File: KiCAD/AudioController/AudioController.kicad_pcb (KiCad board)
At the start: 2 copper layers, 170 x 170 mm, 95 parts, among them J1 CS_1_H, J10 SD_3_CTRL, J11 8P8C, J12 CS_3_Measure, J13 CS_4_H, J14 SD_4_CTRL, J15 8P8C, J16 CS_4_Measure, J17 CS_5_H, J18 SD_5_CTRL, J19 8P8C, J2 SD_1_CTRL, J20 CS_5_Measure, J21 MOSI_H, J22 MOSI_Measure, J23 SCK_H, J24 SCK_Measure, J25 Power, J26 CS1_BR, J27 CS1_BR, J28 CS1_BR, J29 CS1_BR, J3 8P8C, J30 CS1_BR, J4 CS_1_Measure, J5 CS_2_H, J6 SD_2_CTRL, J7 8P8C, J8 CS_2_Measure, J9 CS_3_H, SW1 SW_Push, SW2 SW_Push, SW3 SW_Push, SW4 SW_Push, SW5 SW_Push, SW6 SW_Push, U1 ESP32-DevKitC, U2 ESP32-DevKitC

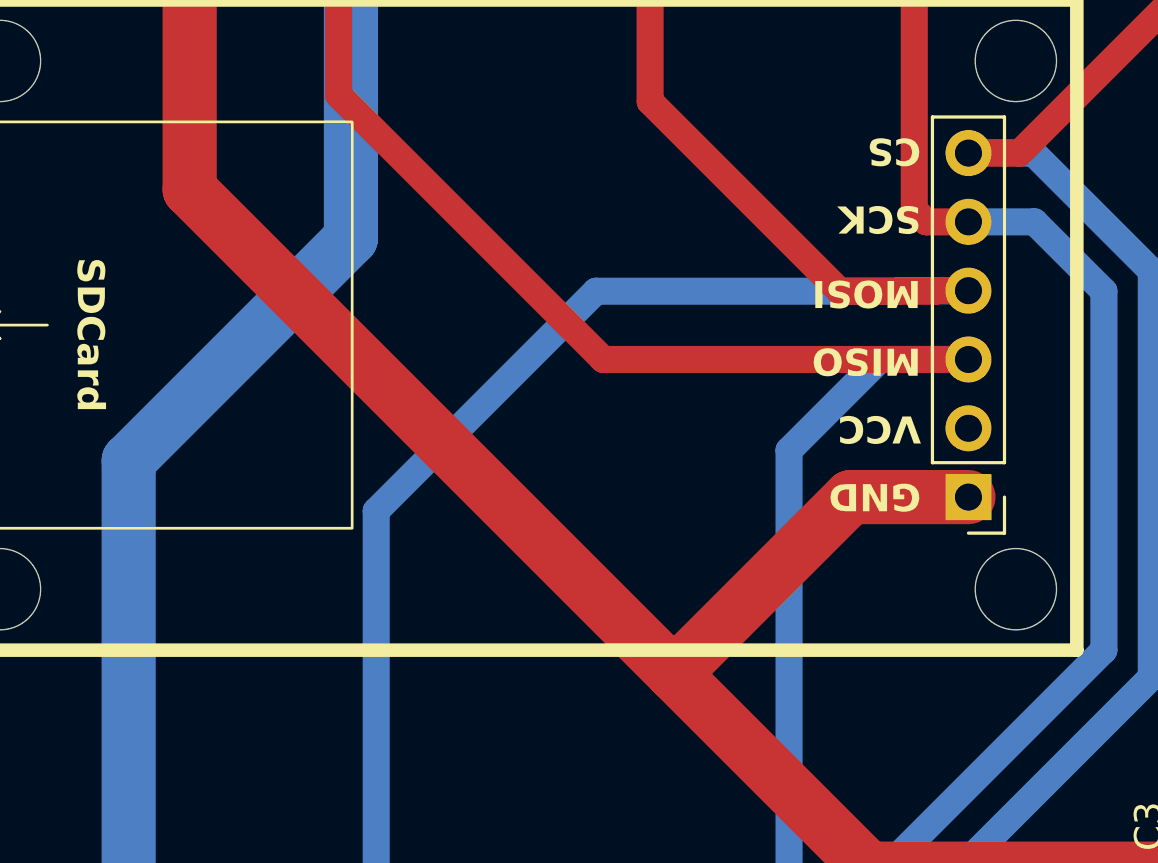
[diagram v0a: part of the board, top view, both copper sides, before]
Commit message: fixed pin assignment sd-card
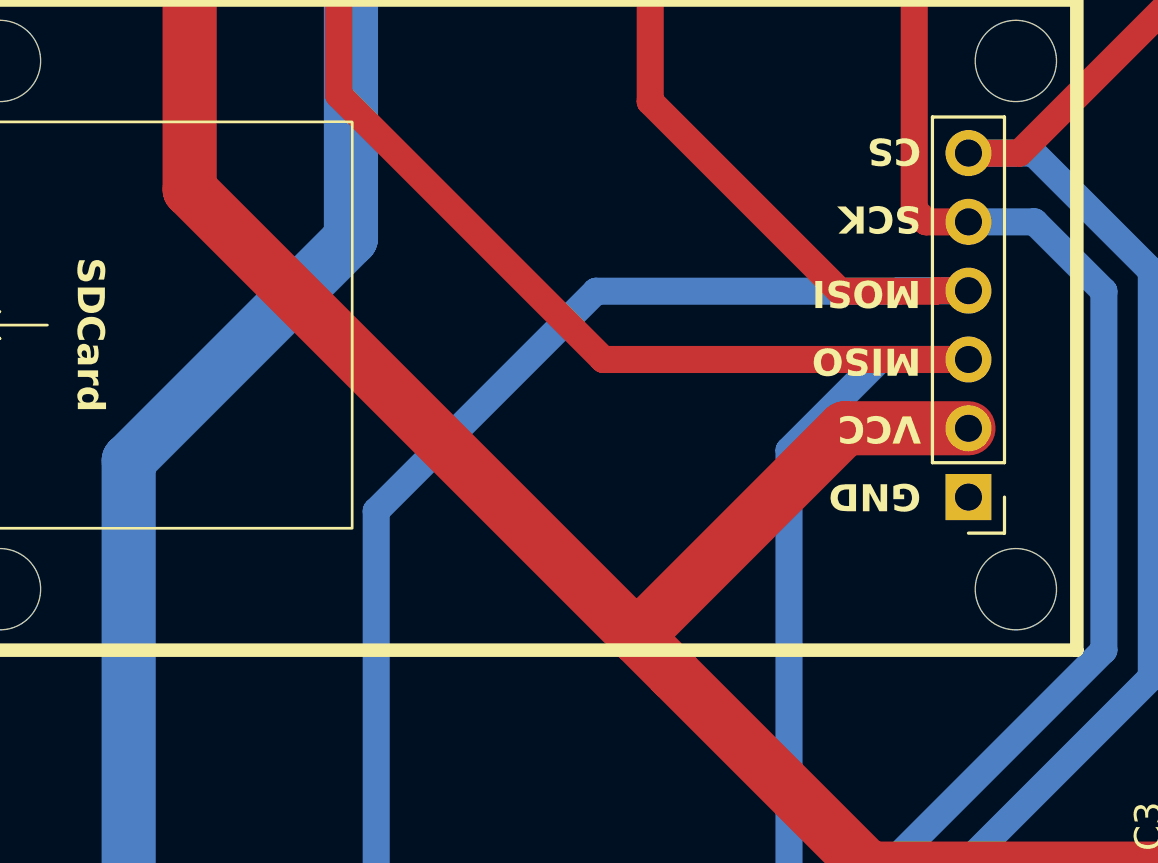
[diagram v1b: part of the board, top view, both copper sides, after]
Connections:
- SD_Card_Reader1 pad 1: +5V -> GND
- SD_Card_Reader1 pad 2: GND -> +5V
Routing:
- net +5V: track 955.9 -> 957.7 mm
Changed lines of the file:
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@@
       (net 12 "/SCK") (pinfunction "In") (pintype "passive"))
     (pad "2" smd custom (at 0 9 270) (size 1 1) (layers "F.Cu" "F.Paste" "F.Mask")
-      (net 2 "GND") (pinfunction "Ext") (pintype "passive") (thermal_bridge_angle 45)
+      (net 2 "GND") (pinfunction "Ext") (pintype "passive")
       (options (clearance outline) (anchor circle))
       (primitives
@@
       ))
     (pad "2" thru_hole custom (at 0 13.75 270) (size 3 3) (drill 1.5) (layers "*.Cu" "*.Mask")
-      (net 2 "GND") (pinfunction "Ext") (pintype "passive") (thermal_bridge_angle 45)
+      (net 2 "GND") (pinfunction "Ext") (pintype "passive")
       (options (clearance outline) (anchor circle))
       (primitives
@@
       (net 15 "/CS_2") (pinfunction "In") (pintype "passive"))
     (pad "2" smd custom (at 0 9 180) (size 1 1) (layers "F.Cu" "F.Paste" "F.Mask")
-      (net 2 "GND") (pinfunction "Ext") (pintype "passive") (thermal_bridge_angle 45)
+      (net 2 "GND") (pinfunction "Ext") (pintype "passive")
       (options (clearance outline) (anchor circle))
       (primitives
@@
       ))
     (pad "2" thru_hole custom (at 0 13.75 180) (size 3 3) (drill 1.5) (layers "*.Cu" "*.Mask")
-      (net 2 "GND") (pinfunction "Ext") (pintype "passive") (thermal_bridge_angle 45)
+      (net 2 "GND") (pinfunction "Ext") (pintype "passive")
       (options (clearance outline) (anchor circle))
       (primitives
@@
       (net 21 "/CS_5") (pinfunction "In") (pintype "passive"))
     (pad "2" smd custom (at 0 9 180) (size 1 1) (layers "F.Cu" "F.Paste" "F.Mask")
-      (net 2 "GND") (pinfunction "Ext") (pintype "passive") (thermal_bridge_angle 45)
+      (net 2 "GND") (pinfunction "Ext") (pintype "passive")
       (options (clearance outline) (anchor circle))
       (primitives
@@
       ))
     (pad "2" thru_hole custom (at 0 13.75 180) (size 3 3) (drill 1.5) (layers "*.Cu" "*.Mask")
-      (net 2 "GND") (pinfunction "Ext") (pintype "passive") (thermal_bridge_angle 45)
+      (net 2 "GND") (pinfunction "Ext") (pintype "passive")
       (options (clearance outline) (anchor circle))
       (primitives
@@
       (net 19 "/CS_4") (pinfunction "In") (pintype "passive"))
     (pad "2" smd custom (at 0 9 180) (size 1 1) (layers "F.Cu" "F.Paste" "F.Mask")
-      (net 2 "GND") (pinfunction "Ext") (pintype "passive") (thermal_bridge_angle 45)
+      (net 2 "GND") (pinfunction "Ext") (pintype "passive")
       (options (clearance outline) (anchor circle))
       (primitives
@@
       ))
     (pad "2" thru_hole custom (at 0 13.75 180) (size 3 3) (drill 1.5) (layers "*.Cu" "*.Mask")
-      (net 2 "GND") (pinfunction "Ext") (pintype "passive") (thermal_bridge_angle 45)
+      (net 2 "GND") (pinfunction "Ext") (pintype "passive")
       (options (clearance outline) (anchor circle))
       (primitives
@@
       (net 11 "/CS_1") (pinfunction "In") (pintype "passive"))
     (pad "2" smd custom (at 0 9 180) (size 1 1) (layers "F.Cu" "F.Paste" "F.Mask")
-      (net 2 "GND") (pinfunction "Ext") (pintype "passive") (thermal_bridge_angle 45)
+      (net 2 "GND") (pinfunction "Ext") (pintype "passive")
       (options (clearance outline) (anchor circle))
       (primitives
@@
       ))
     (pad "2" thru_hole custom (at 0 13.75 180) (size 3 3) (drill 1.5) (layers "*.Cu" "*.Mask")
-      (net 2 "GND") (pinfunction "Ext") (pintype "passive") (thermal_bridge_angle 45)
+      (net 2 "GND") (pinfunction "Ext") (pintype "passive")
       (options (clearance outline) (anchor circle))
       (primitives
@@
     (pad "" np_thru_hole circle (at 33.75 9.75 180) (size 3 3) (drill 3) (layers "F&B.Cu" "*.Mask"))
     (pad "1" thru_hole rect (at -2 -6.35 180) (size 1.7 1.7) (drill 1) (layers "*.Cu" "*.Mask")
-      (net 1 "+5V") (pinfunction "GND") (pintype "passive"))
+      (net 2 "GND") (pinfunction "GND") (pintype "passive"))
     (pad "2" thru_hole oval (at -2 -3.81 180) (size 1.7 1.7) (drill 1) (layers "*.Cu" "*.Mask")
-      (net 2 "GND") (pinfunction "VCC") (pintype "passive"))
+      (net 1 "+5V") (pinfunction "VCC") (pintype "passive"))
     (pad "3" thru_hole oval (at -2 -1.27 180) (size 1.7 1.7) (drill 1) (layers "*.Cu" "*.Mask")
       (net 35 "/SD_MISO") (pinfunction "MISO") (pintype "passive"))
@@
       (net 13 "/MOSI") (pinfunction "In") (pintype "passive"))
     (pad "2" smd custom (at 0 9 270) (size 1 1) (layers "F.Cu" "F.Paste" "F.Mask")
-      (net 2 "GND") (pinfunction "Ext") (pintype "passive") (thermal_bridge_angle 45)
+      (net 2 "GND") (pinfunction "Ext") (pintype "passive")
       (options (clearance outline) (anchor circle))
       (primitives
@@
       ))
     (pad "2" thru_hole custom (at 0 13.75 270) (size 3 3) (drill 1.5) (layers "*.Cu" "*.Mask")
-      (net 2 "GND") (pinfunction "Ext") (pintype "passive") (thermal_bridge_angle 45)
+      (net 2 "GND") (pinfunction "Ext") (pintype "passive")
       (options (clearance outline) (anchor circle))
       (primitives
@@
       (net 17 "/CS_3") (pinfunction "In") (pintype "passive"))
     (pad "2" smd custom (at 0 9 180) (size 1 1) (layers "F.Cu" "F.Paste" "F.Mask")
-      (net 2 "GND") (pinfunction "Ext") (pintype "passive") (thermal_bridge_angle 45)
+      (net 2 "GND") (pinfunction "Ext") (pintype "passive")
       (options (clearance outline) (anchor circle))
       (primitives
@@
       ))
     (pad "2" thru_hole custom (at 0 13.75 180) (size 3 3) (drill 1.5) (layers "*.Cu" "*.Mask")
-      (net 2 "GND") (pinfunction "Ext") (pintype "passive") (thermal_bridge_angle 45)
+      (net 2 "GND") (pinfunction "Ext") (pintype "passive")
       (options (clearance outline) (anchor circle))
       (primitives
@@
     (pts (xy 130 53) (xy 130 223))
     (height 8)
-    (gr_text "170,0000 mm" (at 120.85 138 90) (layer "User.1")
+    (gr_text "170.0000 mm" (at 120.85 138 90) (layer "User.1")
       (effects (font (size 1 1) (thickness 0.15)))
     )
@@
     (pts (xy 130 53) (xy 300 53))
     (height -6)
-    (gr_text "170,0000 mm" (at 215 45.85) (layer "User.1")
+    (gr_text "170.0000 mm" (at 215 45.85) (layer "User.1")
       (effects (font (size 1 1) (thickness 0.15)))
     )
@@
   (segment (start 193.5 155.75) (end 193.5 145.015) (width 2) (layer "F.Cu") (net 1))
   (segment (start 185.25 142.75) (end 178.0625 142.75) (width 2) (layer "F.Cu") (net 1))
-  (segment (start 169 129.6) (end 164.65 129.6) (width 2) (layer "F.Cu") (net 1))
   (segment (start 163.5 220.5) (end 163 221) (width 1) (layer "F.Cu") (net 1))
   (segment (start 289.340938 79.185) (end 291.935 79.185) (width 2) (layer "F.Cu") (net 1))
   (segment (start 146.25 219.5) (end 147.75 221) (width 1) (layer "F.Cu") (net 1))
+  (segment (start 164.44 127.06) (end 156.75 134.75) (width 2) (layer "F.Cu") (net 1))
   (segment (start 287.510938 142.48) (end 289.340938 140.65) (width 2) (layer "F.Cu") (net 1))
   (segment (start 146.5 84.044887) (end 146.205113 83.75) (width 2) (layer "F.Cu") (net 1))
-  (segment (start 158.125 136.125) (end 140.25 118.25) (width 2) (layer "F.Cu") (net 1))
   (segment (start 152.75 220.75) (end 152.5 221) (width 1) (layer "F.Cu") (net 1))
   (segment (start 167.75 218) (end 167.75 220.5) (width 1) (layer "F.Cu") (net 1))
@@
   (segment (start 295.75 202.5) (end 295.75 207.25) (width 2) (layer "F.Cu") (net 1))
   (segment (start 284.275 86.4125) (end 281.6875 89) (width 1) (layer "F.Cu") (net 1))
+  (segment (start 158.125 136.125) (end 156.75 134.75) (width 2) (layer "F.Cu") (net 1))
   (segment (start 284.275 173.195) (end 284.275 178.725) (width 1) (layer "F.Cu") (net 1))
   (segment (start 284.275 117.225) (end 281.75 119.75) (width 1) (layer "F.Cu") (net 1))
@@
   (segment (start 281.735 110.495) (end 283.005 110.495) (width 1) (layer "F.Cu") (net 1))
   (segment (start 209.25 220.75) (end 209.5 221) (width 1) (layer "F.Cu") (net 1))
+  (segment (start 156.75 134.75) (end 140.25 118.25) (width 2) (layer "F.Cu") (net 1))
   (segment (start 291.935 79.185) (end 295.75 83) (width 2) (layer "F.Cu") (net 1))
   (segment (start 287.510938 173.195) (end 289.340938 171.365) (width 2) (layer "F.Cu") (net 1))
@@
   (segment (start 295.75 83) (end 295.75 109.75) (width 2) (layer "F.Cu") (net 1))
   (segment (start 289.525938 109.75) (end 295.75 109.75) (width 2) (layer "F.Cu") (net 1))
-  (segment (start 164.65 129.6) (end 158.125 136.125) (width 2) (layer "F.Cu") (net 1))
   (segment (start 281.735 141.21) (end 283.005 141.21) (width 1) (layer "F.Cu") (net 1))
+  (segment (start 169 127.06) (end 164.44 127.06) (width 2) (layer "F.Cu") (net 1))
   (segment (start 283.005 171.925) (end 284.275 173.195) (width 1) (layer "F.Cu") (net 1))
   (segment (start 287.510938 111.765) (end 289.525938 109.75) (width 2) (layer "F.Cu") (net 1))

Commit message: routed audio controller + added jlc string
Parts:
- removed D1, D2, D3, D5, D7: LED, LED_THT:LED_D5.0mm
- removed R10, R11, R12, R13, R14, R9: 1k, Resistor_SMD:R_0805_2012Metric_Pad1.20x1.40mm_HandSolder
- removed SW5, SW6: SW_Push, Button_Switch_THT:SW_PUSH_6mm
- added C17: 100nF, Capacitor_SMD:C_1206_3216Metric_Pad1.33x1.80mm_HandSolder, F.Cu at (141.5, 191.5)
- added C18: 100nF, Capacitor_SMD:C_1206_3216Metric_Pad1.33x1.80mm_HandSolder, F.Cu at (220.5, 179.5)
- added C19: 100nF, Capacitor_SMD:C_1206_3216Metric_Pad1.33x1.80mm_HandSolder, F.Cu at (197.0, 197.0)
- added D10: WS2812B, LED_SMD:LED_WS2812B_PLCC4_5.0x5.0mm_P3.2mm, F.Cu at (190.1, 191.3)
- added D11: WS2812B, LED_SMD:LED_WS2812B_PLCC4_5.0x5.0mm_P3.2mm, F.Cu at (190.1, 202.8)
- added D12: WS2812B, LED_SMD:LED_WS2812B_PLCC4_5.0x5.0mm_P3.2mm, F.Cu at (176.3, 202.8)
- added D13: WS2812B, LED_SMD:LED_WS2812B_PLCC4_5.0x5.0mm_P3.2mm, F.Cu at (163.3, 203.0)
- added D14: WS2812B, LED_SMD:LED_WS2812B_PLCC4_5.0x5.0mm_P3.2mm, F.Cu at (149.8, 203.0)
- added D15: WS2812B, LED_SMD:LED_WS2812B_PLCC4_5.0x5.0mm_P3.2mm, F.Cu at (213.1, 189.7)
- added D17: WS2812B, LED_SMD:LED_WS2812B_PLCC4_5.0x5.0mm_P3.2mm, F.Cu at (213.2, 199.8)
- added D19: WS2812B, LED_SMD:LED_WS2812B_PLCC4_5.0x5.0mm_P3.2mm, F.Cu at (213.1, 210.3)
- added D9: WS2812B, LED_SMD:LED_WS2812B_PLCC4_5.0x5.0mm_P3.2mm, F.Cu at (176.3, 191.3)
- added J31: Power Bridge, Connector_PinHeader_2.54mm:PinHeader_1x02_P2.54mm_Vertical, F.Cu at (195.5, 152.0)
- added J32: Power Bridge, Connector_PinHeader_2.54mm:PinHeader_1x02_P2.54mm_Vertical, F.Cu at (195.5, 174.2)
- added J33: MOSI Bridge, Connector_PinHeader_2.54mm:PinHeader_1x02_P2.54mm_Vertical, F.Cu at (191.5, 80.5)
- added J34: Pin Bridge, Connector_PinHeader_2.54mm:PinHeader_2x02_P2.54mm_Vertical, F.Cu at (137.7, 140.2)
- added JP2: SJ_C_C2, Jumper:SolderJumper-2_P1.3mm_Open_Pad1.0x1.5mm, F.Cu at (203.3, 159.0)
- added JP3: SJ_C_C3, Jumper:SolderJumper-2_P1.3mm_Open_Pad1.0x1.5mm, F.Cu at (215.3, 154.0)
- added JP4: SJ_C_C4, Jumper:SolderJumper-2_P1.3mm_Open_Pad1.0x1.5mm, F.Cu at (203.3, 154.0)
- added JP5: SJ_C_C1, Jumper:SolderJumper-2_P1.3mm_Open_Pad1.0x1.5mm, F.Cu at (215.3, 159.0)
- added RV1: R_MOSI, Potentiometer_THT:Potentiometer_Piher_PT-6-V_Vertical, F.Cu at (167.6, 84.4)
- added SW7: POWER_SW, Library:Goobay10020, F.Cu at (143.2, 70.1)
- added TP11: COM_C2, TestPoint:TestPoint_Pad_D3.0mm, F.Cu at (206.5, 163.5)
- added TP12: COM_C3, TestPoint:TestPoint_Pad_D3.0mm, F.Cu at (218.0, 148.0)
- added TP13: COM_C4, TestPoint:TestPoint_Pad_D3.0mm, F.Cu at (206.0, 148.0)
- added TP14: COM_C1, TestPoint:TestPoint_Pad_D3.0mm, F.Cu at (218.5, 163.5)
- added TP15: LED_AP, TestPoint:TestPoint_Pad_D3.0mm, F.Cu at (206.5, 170.5)
- added TP16: LED_AB, TestPoint:TestPoint_Pad_D3.0mm, F.Cu at (135.5, 185.5)
- D4, D6, D8: value LED -> WS2812B; footprint LED_THT:LED_D5.0mm -> LED_SMD:LED_WS2812B_PLCC4_5.0x5.0mm_P3.2mm
- J26: value CS1_BR -> CS1_CTRL; footprint Connector_PinHeader_2.54mm:PinHeader_1x02_P2.54mm_Vertical -> Connector_PinHeader_2.54mm:PinHeader_1x03_P2.54mm_Vertical
- J27: value CS1_BR -> CS2_CTRL; footprint Connector_PinHeader_2.54mm:PinHeader_1x02_P2.54mm_Vertical -> Connector_PinHeader_2.54mm:PinHeader_1x03_P2.54mm_Vertical
- J28: value CS1_BR -> CS3_CTRL; footprint Connector_PinHeader_2.54mm:PinHeader_1x02_P2.54mm_Vertical -> Connector_PinHeader_2.54mm:PinHeader_1x03_P2.54mm_Vertical
- J29: value CS1_BR -> CS4_CTRL; footprint Connector_PinHeader_2.54mm:PinHeader_1x02_P2.54mm_Vertical -> Connector_PinHeader_2.54mm:PinHeader_1x03_P2.54mm_Vertical
- J30: value CS1_BR -> CS5_CTRL; footprint Connector_PinHeader_2.54mm:PinHeader_1x02_P2.54mm_Vertical -> Connector_PinHeader_2.54mm:PinHeader_1x03_P2.54mm_Vertical
- JP1: value SolderJumper_2_Open -> PWR_JMP
- R1, R2, R3, R4, R5, R6, R7, R8: value 1k -> 10k
- TP1: value SD_Card_MISO -> SD_MISO
- TP10: value TP_5V -> 5V
- TP2: value SD_Card_MOSI -> SD_MOSI
- TP3: value SD_Card_SCK -> SD_SCK
- TP4: value SD_Card_CS -> SD_CS
- moved R8 79.1 mm to (221.0, 159.0), turned to 0 degrees
- moved D4 67.1 mm to (213.2, 179.7), turned to 180 degrees
- moved R6 63.3 mm to (221.0, 154.0), turned to 0 degrees
- moved R7 59.3 mm to (209.0, 159.0), turned to 0 degrees
- moved D6 54.2 mm to (149.7, 191.5), turned to 180 degrees
- moved R5 47.4 mm to (209.0, 154.0), turned to 0 degrees
- moved D8 40.9 mm to (163.2, 191.5), turned to 180 degrees
- moved JP1 37.8 mm to (145.2, 56.6), turned to 180 degrees
- moved C1 22.4 mm to (195.9, 169.0), turned to 0 degrees
- moved C2 20.8 mm to (194.8, 163.0), turned to 0 degrees
- moved TP9 17.2 mm to (221.0, 65.0)
- moved J22 15.1 mm to (173.4, 62.7)
- moved TP4 10.8 mm to (168.0, 101.0)
- moved R4 9.09 mm to (142.5, 215.5), turned to 90 degrees
- moved TP3 8.75 mm to (159.8, 101.0)
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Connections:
- C5 pad 1: +5V -> Net-(J25-Pin_2)
- C6 pad 1: +5V -> Net-(J25-Pin_2)
- D4 pad 1: GND -> +5V
- D4 pad 2: Net-(D4-A) -> Net-(D15-DIN)
- D6 pad 1: GND -> +5V
- D6 pad 2: Net-(D6-A) -> Net-(D6-DOUT)
- D8 pad 1: GND -> +5V
- J25 pad 2: +5V -> Net-(J25-Pin_2)
- J26 pad 1: /CS_1 -> Net-(J26-Pin_1)
- J26 pad 2: /CS -> /CS_1
- J27 pad 1: /CS_2 -> Net-(J27-Pin_1)
- J27 pad 2: /CS -> /CS_2
- J28 pad 1: /CS_3 -> Net-(J28-Pin_1)
- J28 pad 2: /CS -> /CS_3
- J29 pad 1: /CS_4 -> Net-(J29-Pin_1)
- J29 pad 2: /CS -> /CS_4
- J30 pad 1: /CS_5 -> Net-(J30-Pin_1)
- J30 pad 2: /CS -> /CS_5
- JP1 pad 1: /MOSI -> Net-(J25-Pin_2)
- JP1 pad 2: /MOSI_ESP -> +5V
- R5 pad 2: Net-(D1-A) -> GND
- R6 pad 2: Net-(D2-A) -> GND
- R7 pad 2: Net-(D3-A) -> GND
- R8 pad 1: /LED -> Net-(JP5-B)
- R8 pad 2: Net-(D4-A) -> GND
- U1 pad 19: +5V -> Net-(J32-Pin_2)
- U1 pad 24: unconnected-(U1-ADC2_CH2/GPIO2-Pad24) -> Net-(JP5-B)
- U1 pad 26: unconnected-(U1-ADC2_CH0/GPIO4-Pad26) -> /BTN_3
- U1 pad 3: /BTN_3 -> unconnected-(U1-SENSOR_VP/GPIO36/ADC1_CH0-Pad3)
- U1 pad 33: unconnected-(U1-GPIO21-Pad33) -> /BTN_2
- U1 pad 36: /BTN_2 -> Net-(D6-DIN)
- U1 pad 4: /LED -> unconnected-(U1-SENSOR_VN/GPIO39/ADC1_CH3-Pad4)
- U1 pad 7: unconnected-(U1-32K_XP/GPIO32/ADC1_CH4-Pad7) -> Net-(J34-Pin_1)
- U1 pad 8: unconnected-(U1-32K_XN/GPIO33/ADC1_CH5-Pad8) -> Net-(J34-Pin_3)
- U2 pad 10: /CS_4 -> Net-(J29-Pin_1)
- U2 pad 11: /CS_5 -> Net-(J30-Pin_1)
- U2 pad 19: +5V -> Net-(J31-Pin_2)
- U2 pad 24: /BTN_5 -> /COM_C1
- U2 pad 33: /CS_1 -> Net-(J27-Pin_1)
- U2 pad 36: /CS_2 -> Net-(J26-Pin_1)
- U2 pad 5: Net-(U2-VDET_1/GPIO34/ADC1_CH6) -> /COM_C3
- U2 pad 6: Net-(U2-VDET_2/GPIO35/ADC1_CH7) -> /COM_C4
- U2 pad 7: /BTN_6 -> Net-(D4-DIN)
- U2 pad 8: unconnected-(U2-32K_XN/GPIO33/ADC1_CH5-Pad8) -> /COM_C2
- U2 pad 9: /CS_3 -> Net-(J28-Pin_1)
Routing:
- net +5V: track 957.7 -> 1260.0 mm, vias 0 -> 1
- net Net-(J30-Pin_1): track 0.00 -> 116.4 mm
- net /BTN_6: track 111.1 -> 0.00 mm
- net /CS_5: track 192.3 -> 84.3 mm
- net /BTN_5: track 96.7 -> 0.00 mm
- net Net-(D4-DIN): track 0.00 -> 88.9 mm
- net Net-(J29-Pin_1): track 0.00 -> 88.1 mm
- net Net-(U2-VDET_1/GPIO34/ADC1_CH6): track 80.5 -> 0.00 mm
- net /CS_4: track 164.1 -> 84.2 mm
- net Net-(U2-VDET_2/GPIO35/ADC1_CH7): track 75.7 -> 0.00 mm
- net Net-(D6-DIN): track 0.00 -> 72.8 mm
- net Net-(J28-Pin_1): track 0.00 -> 71.0 mm
- net Net-(J34-Pin_3): track 0.00 -> 68.2 mm, vias 0 -> 1
- net Net-(J34-Pin_1): track 0.00 -> 68.0 mm, vias 0 -> 1
- net /COM_C3: track 0.00 -> 62.0 mm
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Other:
- board text added: "AUDIO CONTROLLER V2.0"
- board text added: "Author: Alexander Hold Version: 2.0"
- board text added: "BR_AB32-AP36"
- board text added: "BR_AB33-AP39"
- board text added: "BR_PWR_SW"
- board text added: "CS1"
- board text added: "CS2"
- board text added: "CS3"
- board text added: "CS4"
- board text added: "CS5"
- board text added: "OFF"
- board text added: "ON"
- board text added: "PWR_ESP"
- board text added: "S_CS"
- board text removed: "AUDIO CONTROLLER V1.0"
- board text removed: "Author: Alexander Hold Version: 1.0"
- board text removed: "CS BNC"
- board text removed: "Controls: Audio Buffer"
- board text removed: "Controls: Audio Player"
